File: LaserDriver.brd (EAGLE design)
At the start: 64.4 x 21.6 mm, 13 parts

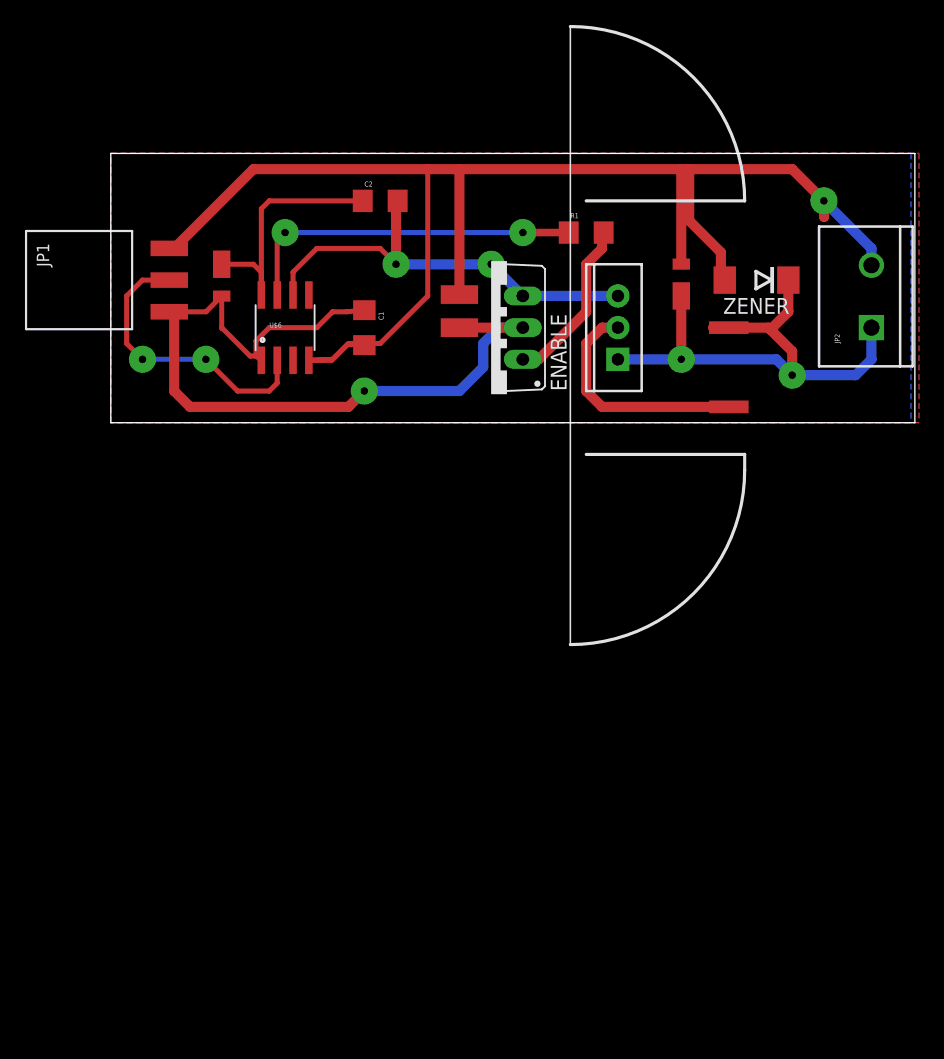
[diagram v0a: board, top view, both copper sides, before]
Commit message: revised for capacitive loads
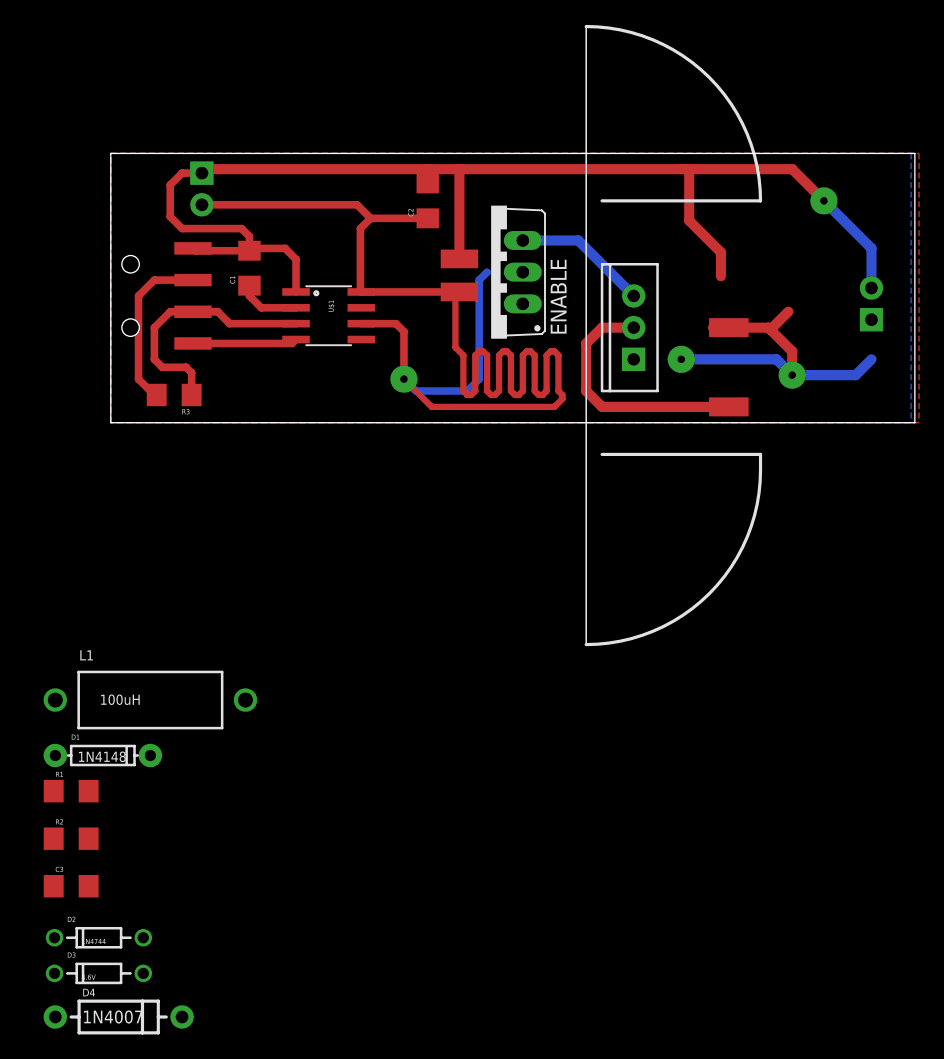
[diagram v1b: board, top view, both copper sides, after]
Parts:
- removed DRIVER_DIODE, OVERVOLT_PROTECTION: DFLS1150, hmcfabstudio:2SMD_FLAT_LEAD
- removed JP1: 1x3 RA Female .1", SparkFun-Connectors:1X03_SMD_RA_FEMALE
- removed JP2: M025MM, SparkFun-Connectors:SCREWTERMINAL-5MM-2
- removed U$6: IR2101, hmcfabstudio:SO08
- removed ZENER: PTZTE254.3BCT-ND, diode:DO214AA
- added C3: 10uF, SparkFun-Capacitors:1206
- added D1: 1N4148, SparkFun-DiscreteSemi:DIODE-1N4148
- added D2: 1N4744, SparkFun-DiscreteSemi:DIODE-ZENER
- added D3: 4.6V, SparkFun-DiscreteSemi:DIODE-ZENER
- added D4: 1N4007, SparkFun-DiscreteSemi:DIODE-1N4001-KIT
- added JP3, JP4: M02POLAR, SparkFun-Connectors:MOLEX-1X2
- added JP5: (no value), SparkFun-Connectors:1X04-SMD
- added L1: 100uH, SparkFun-Passives:AXIAL-0.6
- added R2, R3: 10k, SparkFun-Passives:1206
- added U$1: LT1910, hmcfabstudio:SO08
- C1: value 10uF -> .1uF
- R1: value (none) -> 10k
- RSMF2JT1R00: value PWR_RESISTOR -> 2W
- moved R1 60.9 mm to (-3.17, -29.5)
- moved C1 10.4 mm to (11.1, 12.4), turned to 90 degrees
- moved ENABLE 4.44 mm to (30.5, 12.1)
- moved C2 3.81 mm to (25.4, 17.8), turned to 90 degrees
- moved BYPASS_CAP 2.86 mm to (27.9, 10.5)
- moved U$2 1.27 mm to (41.9, 7.62)
- renumbered U$5 to RSMF2JT1R00
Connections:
- removed net N$8: JP2.1, OVERVOLT_PROTECTION.C, RSMF2JT1R00.P$1, U$2.ADJ, ZENER.C
- new net N$1: JP4.1, L1.P$2
- new net N$10: D1.C, R1.2, U$1.5
- new net N$11: D3.P$1, D4.C, L1.P$1, RSMF2JT1R00.P$1, U$2.ADJ
- new net N$3: C1.1, U$1.2
- new net VDD: JP5.2, R3.2
- net GND: now also C2.2, C3.2, D3.P$2, D4.A, JP3.1, JP4.2, JP5.1, U$1.1; no longer JP1.1, JP2.2, OVERVOLT_PROTECTION.A, U$6.4, ZENER.A
- net N$2: now also JP5.3, R3.1, U$1.3; no longer C2.1, DRIVER_DIODE.C, U$6.8
- net N$4: now also D2.P$2; no longer C2.2, U$6.6
- net N$5: now also C3.1, R2.2; no longer U$6.7
- net N$6: now also D1.A, D2.P$1, R2.1; no longer R1.2
- net N$9: now also JP5.4, U$1.4; no longer JP1.2, U$6.2
- net VIN: now also C2.1, JP3.2, U$1.6, U$1.8; no longer C1.1, DRIVER_DIODE.A, JP1.3, U$6.1
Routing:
- net VIN: track 66.2 -> 111.1 mm
- net N$8: track 42.6 -> 0.00 mm, vias 2 -> 0
- net N$5: track 28.0 -> 0.00 mm, vias 2 -> 0
- net N$11: track 0.00 -> 27.4 mm, vias 0 -> 2
- net N$4: track 35.4 -> 10.7 mm, vias 2 -> 0
- net GND: track 120.1 -> 103.0 mm
- net N$9: track 23.5 -> 8.39 mm, vias 2 -> 0
- net N$6: track 13.6 -> 0.00 mm
- net VDD: track 0.00 -> 13.5 mm
- net N$3: track 0.00 -> 4.95 mm
- net N$7: track 18.8 -> 20.1 mm
- net N$2: track 20.6 -> 20.0 mm
